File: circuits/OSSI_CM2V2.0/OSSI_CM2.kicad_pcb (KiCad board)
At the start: 4 copper layers, 49.5 x 54.9 mm, 80 parts, among them U101 STM32L412C8T6, U102 M24M01, U103 LM75B, U104 OPA2317, X101 PINHEADER_2×5, X201 Conn_01x20_Pin, X202 Conn_01x21_Pin, Y101 10MHz

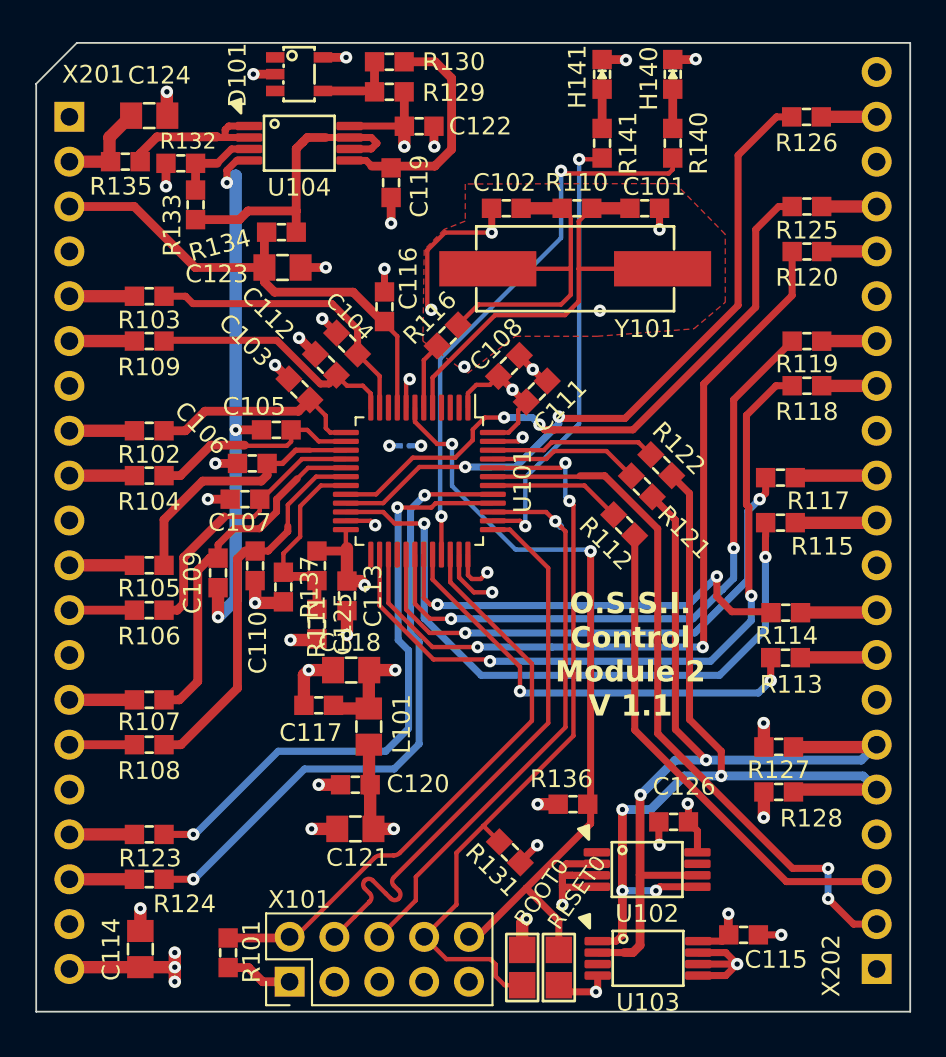
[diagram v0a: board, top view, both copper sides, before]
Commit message: cleans up routing, library links, library 3D models
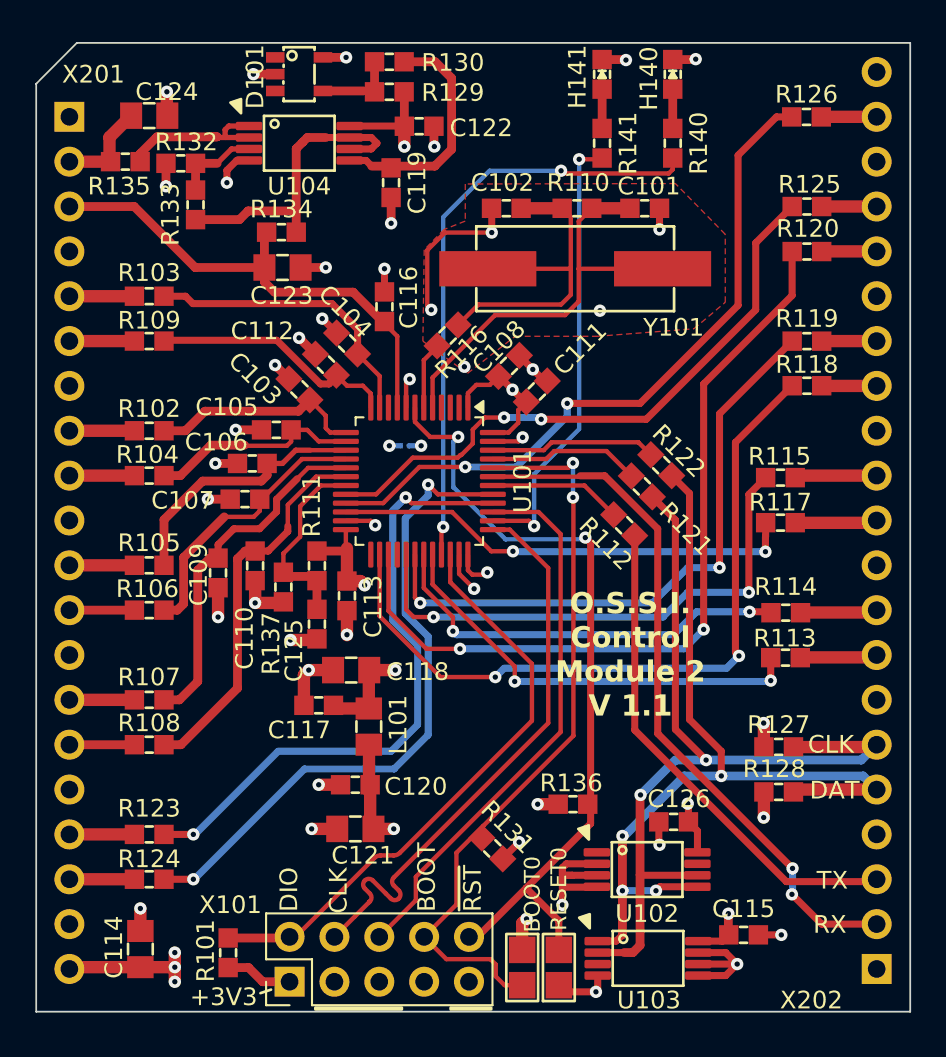
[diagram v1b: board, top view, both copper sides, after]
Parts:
- C101, C102, C103, C104, C105, C106, C107, C108, C109, C110, C111, C112, C113, C115, C116, C117, C119, C120, C122, C125, C126: footprint OSSI_standard_footprints:0603_W -> OSSI_standard_footprints:0603_W_C
- C114, C118, C121, C123, C124: footprint OSSI_standard_footprints:0805_W -> OSSI_standard_footprints:0805_W_C
- H140: value LED -> LED gn
- H141: value LED -> LED rd
- L101: footprint OSSI_standard_footprints:0805_W -> OSSI_standard_footprints:0805_W_L
- R101, R102, R103, R104, R105, R106, R107, R108, R109, R110, R111, R112, R113, R114, R115, R116, R117, R118, R119, R120, R121, R122, R123, R124, R125, R126, R127, R128, R129, R130, R131, R132, R133, R134, R135, R136, R137, R140, R141: footprint OSSI_standard_footprints:0603_W -> OSSI_standard_footprints:0603_W_R
- moved R131 1.02 mm to (143.3, 118.9)
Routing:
- net AGND: track 57.5 -> 31.4 mm
- net Net-(U101A-PB11/T2Ch4): track 37.9 -> 26.3 mm
- net Net-(U101A-PA12): track 31.7 -> 34.0 mm
- net Net-(U101A-PA9/T1Ch2): track 36.9 -> 35.2 mm
- net Net-(U101A-PB5): track 36.1 -> 37.5 mm
- net GND: track 51.8 -> 50.5 mm
- net Net-(U101A-PB13/T1Ch1N): track 41.2 -> 42.5 mm
- net Net-(U101A-PB4): track 34.6 -> 35.8 mm
- net Net-(U101B-PH3/BOOT0): track 43.1 -> 42.1 mm
- net Net-(U101B-~{RST}): track 44.4 -> 45.4 mm
- net /TRACE_SWO/PB3: track 32.3 -> 31.4 mm, vias 1 -> 0
- net I2C_Dat: track 50.9 -> 50.0 mm
- net Net-(U101A-PA10/T1Ch3): track 24.4 -> 23.6 mm
- net Net-(U101A-PB2): track 35.6 -> 34.8 mm
- net Net-(U101A-PA11/T1Ch4): track 25.6 -> 24.9 mm
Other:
- board text added: "(Boost_T1) PA10"
- board text added: "(Bridge_T2) PB13"
- board text added: "(Bridge_T3) PA9"
- board text added: "(Bridge_T4) PB14"
- board text added: "(Grid_Relay_Ctrl) PB10"
- board text added: "(HISIDE_PWM_µC) PA11"
- board text added: "(I2C_Clk) PB8"
- board text added: "(I2C_Dat) PB9"
- board text added: "(Inv_Relay_Ctrl) PB2"
- board text added: "BOOT"
- board text added: "CLK"
- board text added: "DAT"
- board text added: "DIO"
- board text added: "PB4 (LED_Red_Ctrl)"
- board text added: "PB5 (LED_Green_Ctrl)"
- board text added: "RX"
- board text added: "TX"
- board text added: "~{RST}"
- board text removed: "(Boost_T1) PB10"
- board text removed: "(Bridge_T2) PA9"
- board text removed: "(Bridge_T3) PA10"
- board text removed: "(Bridge_T4) PA11"
- board text removed: "(Grid_Relay_Ctrl) PB8"
- board text removed: "(HISIDE_PWM_µC) PB3"
- board text removed: "(I2C_Clk) PB13"
- board text removed: "(I2C_Dat) PB14"
- board text removed: "(Inv_Relay_Ctrl) PB5"
- board text removed: "PB1 (LED_Red_Ctrl)"
- board text removed: "PB4 (LED_Green_Ctrl)"

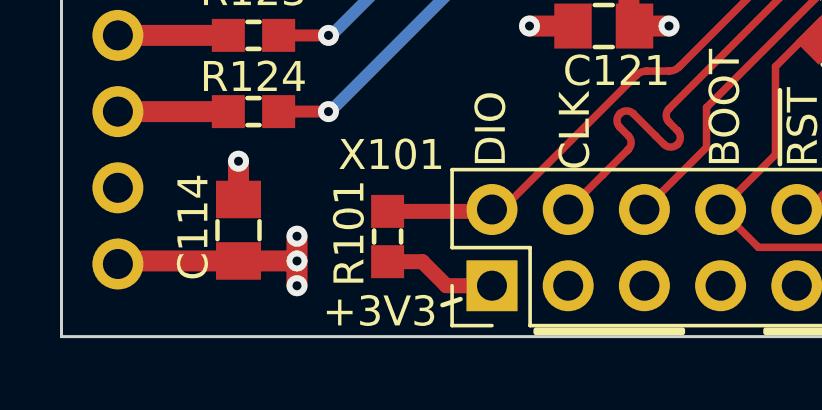
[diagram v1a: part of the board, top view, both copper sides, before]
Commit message: cleans up and rearranges schematics for more clarity
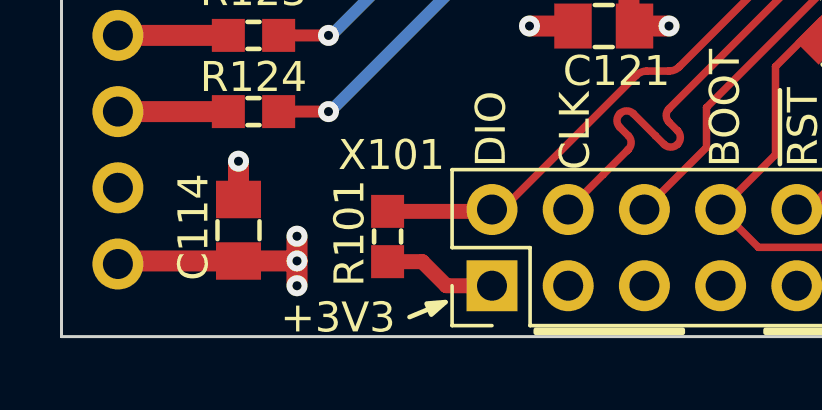
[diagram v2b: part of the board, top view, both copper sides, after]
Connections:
- net Net-(U101B-PH3/BOOT0) renamed /BOOT
- net Net-(U101B-~{RST}) renamed /~{RESET}
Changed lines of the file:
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@@
 	(net 72 "/SWD_CLK{slash}PA14")
 	(net 73 "UART_RX")
-	(net 74 "Net-(U101B-PH3{slash}BOOT0)")
-	(net 75 "Net-(U101B-~{RST})")
+	(net 74 "/BOOT")
+	(net 75 "/~{RESET}")
 	(net 76 "unconnected-(U103-~{O.S.}-Pad3)")
 	(net 77 "unconnected-(X101-Pad7)")
@@
 			(size 1.1 1.1)
 			(layers "F.Cu" "F.Paste" "F.Mask")
-			(net 74 "Net-(U101B-PH3{slash}BOOT0)")
+			(net 74 "/BOOT")
 			(pinfunction "2")
 			(pintype "passive")
@@
 			)
 		)
-		(property "Datasheet" ""
+		(property "Datasheet" "http://www.ti.com/lit/ds/symlink/lm4030.pdf"
 			(at 0 0 -90)
 			(unlocked yes)
@@
 			)
 		)
-		(property "Description" ""
+		(property "Description" "2.5 V shunt voltage reference in SOT-23-5 package"
 			(at 0 0 -90)
 			(unlocked yes)
@@
 			)
 		)
-		(property "Manufacturer" "Texas Instruments"
+		(property "Manufacturer" "M"
 			(at 0 0 180)
 			(layer "F.Fab")
@@
 			)
 		)
+		(sheetname "Root")
+		(sheetfile "OSSI_CM2.kicad_sch")
 		(attr smd)
 		(fp_line
@@
 			(net 19 "Net-(D101-K)")
 			(pinfunction "K")
-			(pintype "bidirectional")
+			(pintype "input")
 		)
 		(pad "5" smd rect
@@
 			(net 4 "AGND")
 			(pinfunction "A")
-			(pintype "bidirectional")
+			(pintype "input")
 		)
 		(model "${KICAD8_3DMODEL_DIR}/Package_TO_SOT_SMD.3dshapes/SOT-23-5.step"
@@
 			(size 1.5 1.5)
 			(layers "F.Cu" "F.Paste" "F.Mask")
-			(net 75 "Net-(U101B-~{RST})")
+			(net 75 "/~{RESET}")
 			(pinfunction "2")
 			(pintype "passive")
@@
 			(size 1.5 1.5)
 			(layers "F.Cu" "F.Paste" "F.Mask")
-			(net 74 "Net-(U101B-PH3{slash}BOOT0)")
+			(net 74 "/BOOT")
 			(pinfunction "2")
 			(pintype "passive")
@@
 			)
 		)
+		(sheetname "Root")
+		(sheetfile "OSSI_CM2.kicad_sch")
 		(attr smd)
 		(fp_line
@@
 			(layers "F.Cu" "F.Paste" "F.Mask")
 			(roundrect_rratio 0.25)
-			(net 75 "Net-(U101B-~{RST})")
+			(net 75 "/~{RESET}")
 			(pinfunction "~{RST}")
 			(pintype "bidirectional")
@@
 			(layers "F.Cu" "F.Paste" "F.Mask")
 			(roundrect_rratio 0.25)
-			(net 74 "Net-(U101B-PH3{slash}BOOT0)")
+			(net 74 "/BOOT")
 			(pinfunction "PH3/BOOT0")
 			(pintype "bidirectional")
@@
 			)
 		)
-		(property "Description" ""
+		(property "Description" "Pin header 2×5 pole"
 			(at 0 0 90)
 			(unlocked yes)
@@
 			(net 10 "+3V3")
 			(pinfunction "1")
-			(pintype "bidirectional")
+			(pintype "passive")
 		)
 		(pad "2" thru_hole oval
@@
 			(net 70 "/SWD_DIO{slash}PA13")
 			(pinfunction "2")
-			(pintype "bidirectional")
+			(pintype "passive")
 		)
 		(pad "3" thru_hole oval
@@
 			(net 1 "GND")
 			(pinfunction "3")
-			(pintype "bidirectional")
+			(pintype "passive")
 		)
 		(pad "4" thru_hole oval
@@
 			(net 72 "/SWD_CLK{slash}PA14")
 			(pinfunction "4")
-			(pintype "bidirectional")
+			(pintype "passive")
 		)
 		(pad "5" thru_hole oval
@@
 			(net 1 "GND")
 			(pinfunction "5")
-			(pintype "bidirectional")
+			(pintype "passive")
 		)
 		(pad "6" thru_hole oval
@@
 			(net 71 "/TRACE_SWO{slash}PB3")
 			(pinfunction "6")
-			(pintype "bidirectional")
+			(pintype "passive")
 		)
 		(pad "7" thru_hole oval
@@
 			(net 77 "unconnected-(X101-Pad7)")
 			(pinfunction "7")
-			(pintype "bidirectional+no_connect")
+			(pintype "passive+no_connect")
 		)
 		(pad "8" thru_hole oval
@@
 			(layers "*.Cu" "*.Mask")
 			(remove_unused_layers no)
-			(net 74 "Net-(U101B-PH3{slash}BOOT0)")
+			(net 74 "/BOOT")
 			(pinfunction "8")
-			(pintype "bidirectional")
+			(pintype "passive")
 		)
 		(pad "9" thru_hole oval
@@
 			(net 1 "GND")
 			(pinfunction "9")
-			(pintype "bidirectional")
+			(pintype "passive")
 		)
 		(pad "10" thru_hole oval
@@
 			(layers "*.Cu" "*.Mask")
 			(remove_unused_layers no)
-			(net 75 "Net-(U101B-~{RST})")
+			(net 75 "/~{RESET}")
 			(pinfunction "10")
-			(pintype "bidirectional")
+			(pintype "passive")
 		)
 		(model "${KICAD6_3DMODEL_DIR}/Connector_PinHeader_2.54mm.3dshapes/PinHeader_2x05_P2.54mm_Vertical.wrl"
@@
 			(size 1.1 1.1)
 			(layers "F.Cu" "F.Paste" "F.Mask")
-			(net 75 "Net-(U101B-~{RST})")
+			(net 75 "/~{RESET}")
 			(pinfunction "2")
 			(pintype "passive")
@@
 	)
 	(gr_line
-		(start 130.8 126.9)
-		(end 130.2 127.1)
+		(start 130.3 127)
+		(end 129.1 127.5)
 		(stroke
 			(width 0.154)
@@
 		(layer "F.SilkS")
 	)
+	(gr_poly
+		(pts
+			(xy 130.3 127) (xy 129.669553 127.050338) (xy 129.825844 127.418538)
+		)
+		(stroke
+			(width 0.154)
+			(type solid)
+		)
+		(fill solid)
+		(layer "F.SilkS")
+	)
 	(gr_rect
 		(start 140.968844 127.924499)
@@
 	)
 	(gr_text "+3V3"
-		(at 126.200002 127.899998 0)
+		(at 124.8 128.1 0)
 		(layer "F.SilkS")
 		(effects
